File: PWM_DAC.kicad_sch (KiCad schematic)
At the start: 26 parts, among them J1 Conn_01x04_Pin, J2 Conn_01x01_Pin, J3 Conn_01x01_Pin, Q2 NPN, U1 LT1054, U2 REF5050ID, U3 OP07, U4 L7805, U5 ESP32-S3-DevKitC

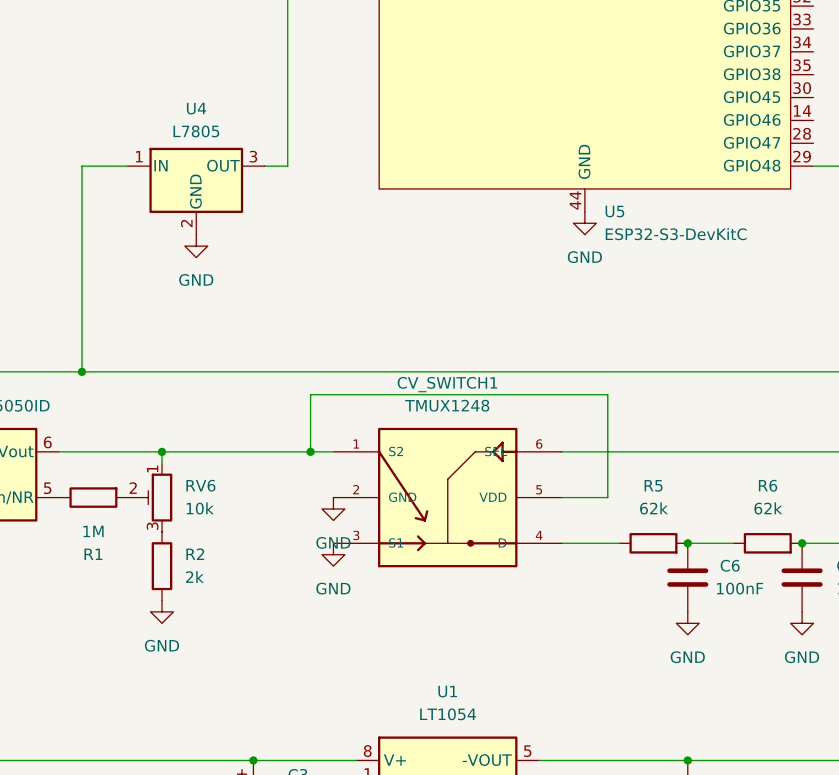
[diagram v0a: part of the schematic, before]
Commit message: Izmenjen deo šeme. Analogni prekidač se sada napaja preko regulatora.
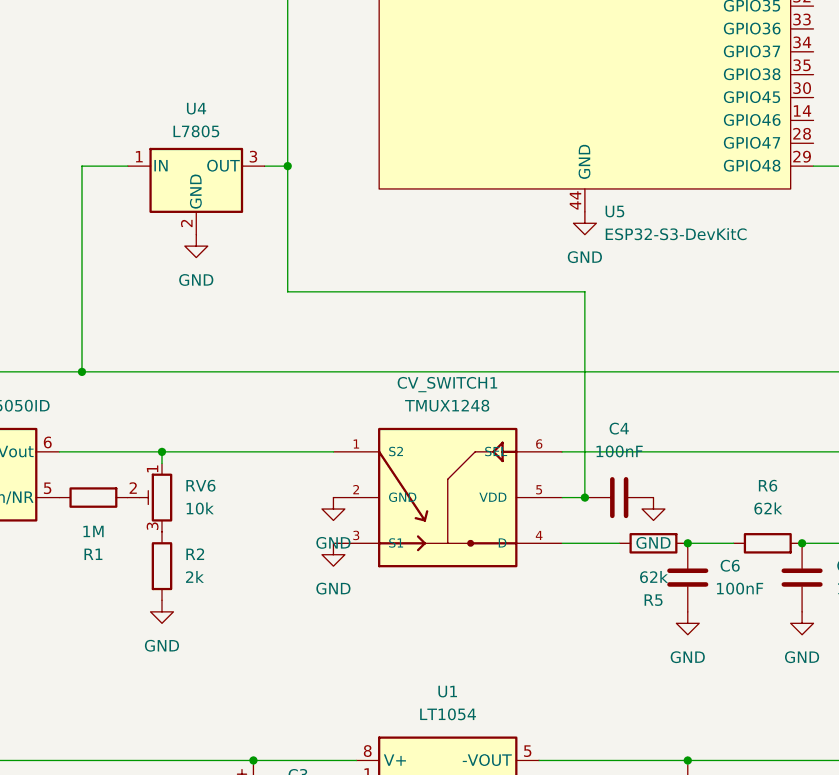
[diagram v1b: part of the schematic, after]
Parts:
- added C4: 100nF, Package_DFN_QFN:DFN-8-1EP_1.5x1.5mm_P0.4mm_EP0.7x1.2mm, symbol Device:C
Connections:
- net GND: now also C4.1
- net at CV_SWITCH1.1 (S2), RV6.1, U2.6 (Vout): no longer CV_SWITCH1.5 (VDD)
- net at U4.3 (OUT), U5.21 (5V): now also CV_SWITCH1.5 (VDD), C4.2
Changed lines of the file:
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@@
 	(paper "User" 406.4 228.6)
 	(junction
-		(at 172.72 139.7)
+		(at 170.18 107.95)
 		(diameter 0)
 		(color 0 0 0 0)
@@
 	)
 	(junction
+		(at 203.2 144.78)
+		(diameter 0)
+		(color 0 0 0 0)
+	)
+	(junction
 		(at 166.37 173.99)
 		(diameter 0)
@@
 	(wire
 		(pts
+			(xy 170.18 107.95) (xy 170.18 121.92)
+		)
+		(stroke
+			(width 0)
+			(type default)
+		)
+	)
+	(wire
+		(pts
 			(xy 250.19 87.63) (xy 250.19 82.55)
 		)
@@
 	(wire
 		(pts
+			(xy 203.2 144.78) (xy 200.66 144.78)
+		)
+		(stroke
+			(width 0)
+			(type default)
+		)
+	)
+	(wire
+		(pts
+			(xy 203.2 121.92) (xy 203.2 144.78)
+		)
+		(stroke
+			(width 0)
+			(type default)
+		)
+	)
+	(wire
+		(pts
 			(xy 237.49 139.7) (xy 200.66 139.7)
 		)
@@
 	(wire
 		(pts
-			(xy 156.21 139.7) (xy 172.72 139.7)
+			(xy 156.21 139.7) (xy 175.26 139.7)
 		)
 		(stroke
@@
 	(wire
 		(pts
-			(xy 205.74 144.78) (xy 205.74 133.35)
+			(xy 265.43 21.59) (xy 274.32 21.59)
 		)
 		(stroke
@@
 	(wire
 		(pts
-			(xy 265.43 21.59) (xy 274.32 21.59)
+			(xy 170.18 121.92) (xy 203.2 121.92)
 		)
 		(stroke
@@
 	(wire
 		(pts
-			(xy 172.72 139.7) (xy 175.26 139.7)
-		)
-		(stroke
-			(width 0)
-			(type default)
-		)
-	)
-	(wire
-		(pts
 			(xy 251.46 160.02) (xy 267.97 160.02)
 		)
@@
 	(wire
 		(pts
-			(xy 200.66 144.78) (xy 205.74 144.78)
-		)
-		(stroke
-			(width 0)
-			(type default)
-		)
-	)
-	(wire
-		(pts
 			(xy 198.12 179.07) (xy 200.66 179.07)
 		)
@@
 	(wire
 		(pts
-			(xy 205.74 133.35) (xy 172.72 133.35)
-		)
-		(stroke
-			(width 0)
-			(type default)
-		)
-	)
-	(wire
-		(pts
 			(xy 241.3 33.02) (xy 241.3 54.61)
 		)
@@
 	(wire
 		(pts
-			(xy 172.72 133.35) (xy 172.72 139.7)
-		)
-		(stroke
-			(width 0)
-			(type default)
-		)
-	)
-	(wire
-		(pts
 			(xy 207.01 149.86) (xy 200.66 149.86)
 		)
@@
 	)
 	(symbol
+		(lib_id "power:GND")
+		(at 210.82 144.78 0)
+		(unit 1)
+		(body_style 1)
+		(exclude_from_sim no)
+		(in_bom yes)
+		(on_board yes)
+		(in_pos_files yes)
+		(dnp no)
+		(fields_autoplaced yes)
+		(property "Reference" "#PWR019"
+			(at 210.82 151.13 0)
+			(hide yes)
+			(show_name no)
+			(do_not_autoplace no)
+			(effects
+				(font
+					(size 1.27 1.27)
+				)
+			)
+		)
+		(property "Value" "GND"
+			(at 210.82 149.86 0)
+			(show_name no)
+			(do_not_autoplace no)
+			(effects
+				(font
+					(size 1.27 1.27)
+				)
+			)
+		)
+		(property "Footprint" ""
+			(at 210.82 144.78 0)
+			(hide yes)
+			(show_name no)
+			(do_not_autoplace no)
+			(effects
+				(font
+					(size 1.27 1.27)
+				)
+			)
+		)
+		(property "Datasheet" ""
+			(at 210.82 144.78 0)
+			(hide yes)
+			(show_name no)
+			(do_not_autoplace no)
+			(effects
+				(font
+					(size 1.27 1.27)
+				)
+			)
+		)
+		(property "Description" "Power symbol creates a global label with name \"GND\" , ground"
+			(at 210.82 144.78 0)
+			(hide yes)
+			(show_name no)
+			(do_not_autoplace no)
+			(effects
+				(font
+					(size 1.27 1.27)
+				)
+			)
+		)
+		(pin "1"
+		)
+		(instances
+			(project "PWM_DAC"
+				(path "/f2f64783-3dc6-46eb-a96d-e5bfedd35fa1"
+					(reference "#PWR019")
+					(unit 1)
+				)
+			)
+		)
+	)
+	(symbol
 		(lib_id "PCM_Espressif:ESP32-S3-DevKitC")
 		(at 203.2 67.31 0)
@@
 	(symbol
 		(lib_id "Device:C")
+		(at 207.01 144.78 270)
+		(unit 1)
+		(body_style 1)
+		(exclude_from_sim no)
+		(in_bom yes)
+		(on_board yes)
+		(in_pos_files yes)
+		(dnp no)
+		(fields_autoplaced yes)
+		(property "Reference" "C4"
+			(at 207.01 137.16 90)
+			(show_name no)
+			(do_not_autoplace no)
+			(effects
+				(font
+					(size 1.27 1.27)
+				)
+			)
+		)
+		(property "Value" "100nF"
+			(at 207.01 139.7 90)
+			(show_name no)
+			(do_not_autoplace no)
+			(effects
+				(font
+					(size 1.27 1.27)
+				)
+			)
+		)
+		(property "Footprint" "Package_DFN_QFN:DFN-8-1EP_1.5x1.5mm_P0.4mm_EP0.7x1.2mm"
+			(at 203.2 145.7452 0)
+			(hide yes)
+			(show_name no)
+			(do_not_autoplace no)
+			(effects
+				(font
+					(size 1.27 1.27)
+				)
+			)
+		)
+		(property "Datasheet" ""
+			(at 207.01 144.78 0)
+			(hide yes)
+			(show_name no)
+			(do_not_autoplace no)
+			(effects
+				(font
+					(size 1.27 1.27)
+				)
+			)
+		)
+		(property "Description" "Unpolarized capacitor"
+			(at 207.01 144.78 0)
+			(hide yes)
+			(show_name no)
+			(do_not_autoplace no)
+			(effects
+				(font
+					(size 1.27 1.27)
+				)
+			)
+		)
+		(pin "1"
+		)
+		(pin "2"
+		)
+		(instances
+			(project "PWM_DAC"
+				(path "/f2f64783-3dc6-46eb-a96d-e5bfedd35fa1"
+					(reference "C4")
+					(unit 1)
+				)
+			)
+		)
+	)
+	(symbol
+		(lib_id "Device:C")
 		(at 264.16 172.72 0)
 		(unit 1)
@@
 		(lib_id "Device:R")
 		(at 210.82 149.86 90)
+		(mirror x)
 		(unit 1)
 		(body_style 1)
@@
 		(in_pos_files yes)
 		(dnp no)
-		(fields_autoplaced yes)
 		(property "Reference" "R5"
-			(at 210.82 143.51 90)
+			(at 210.82 156.21 90)
 			(show_name no)
 			(do_not_autoplace no)
@@
 		)
 		(property "Value" "62k"
-			(at 210.82 146.05 90)
+			(at 210.82 153.67 90)
 			(show_name no)
 			(do_not_autoplace no)
@@
 		)
 		(property "Footprint" ""
-			(at 210.82 151.638 90)
+			(at 210.82 148.082 90)
 			(hide yes)
 			(show_name no)

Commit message: Ispravljena pogrešna vrednost kondenzatora
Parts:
- C1: value 100uF -> 10uF
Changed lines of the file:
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@@
 			)
 		)
-		(property "Value" "100uF"
+		(property "Value" "10uF"
 			(at 204.47 184.5309 0)
 			(show_name no)
